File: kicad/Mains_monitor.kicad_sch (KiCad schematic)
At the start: 31 parts, among them J1 120VAC, J2 LOAD, K1 SANYOU_SRD_Form_C, Q1 NPN, Q2 BS170, T1 CST2010, U1 HLW8032

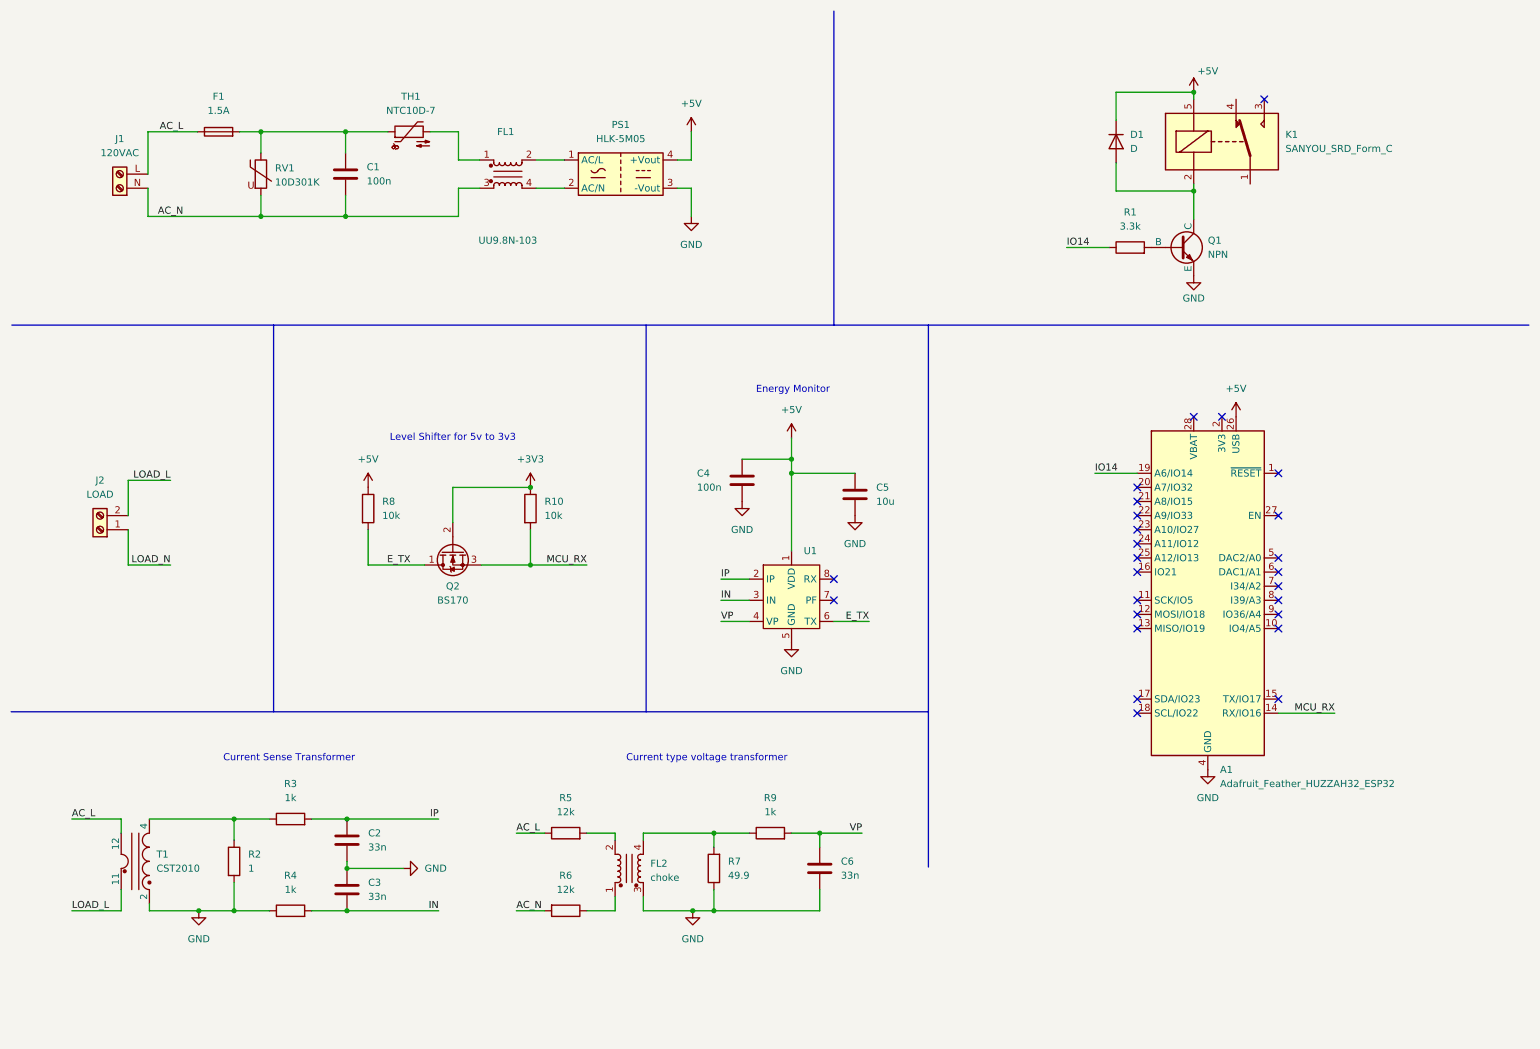
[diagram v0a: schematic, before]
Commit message: Improve sch clarity
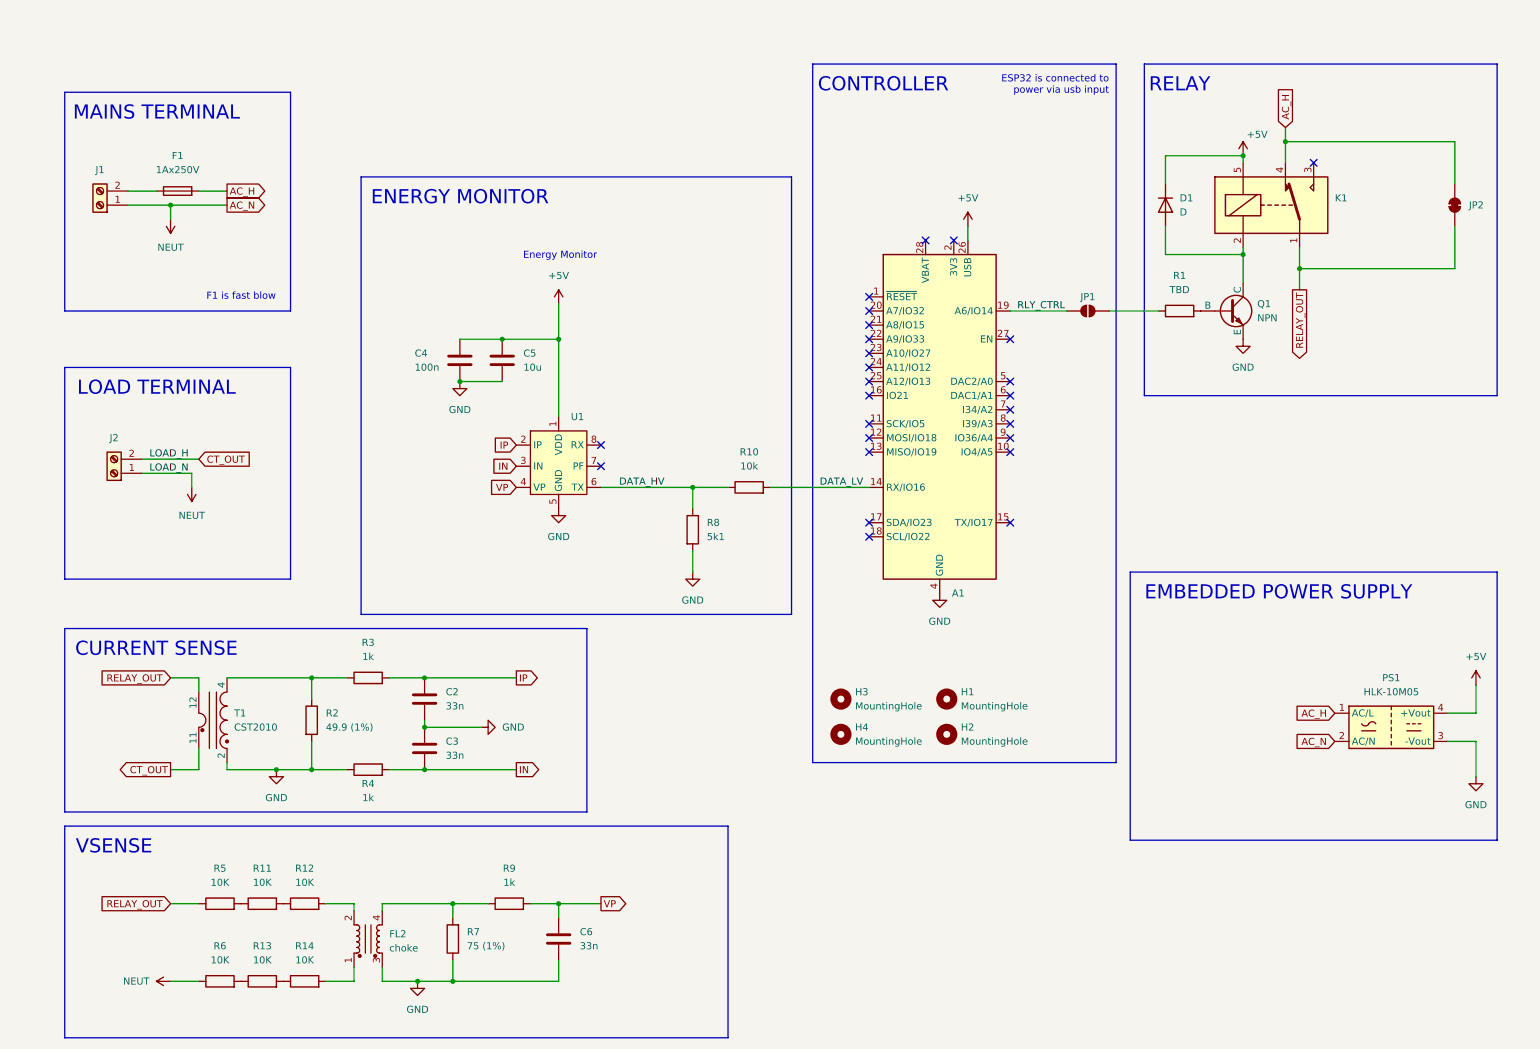
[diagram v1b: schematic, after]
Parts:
- removed C1: 100n, Capacitor_THT:C_Rect_L18.0mm_W5.0mm_P15.00mm_FKS3_FKP3, symbol Device:C
- removed FL1: UU9.8N-103, Inductor_THT:Choke_Schaffner_RN102-04-14.0x14.0mm, symbol Filter:Choke_Schaffner_RN102-0.3-02-12M
- removed PS1: HLK-5M05, Converter_ACDC:Converter_ACDC_Hi-Link_HLK-5Mxx, symbol Converter_ACDC:HLK-5M05
- removed Q2: BS170, Package_TO_SOT_THT:TO-92_Inline, symbol Transistor_FET:BS170
- removed RV1: 10D301K, symbol Device:Varistor
- removed TH1: NTC10D-7, symbol Device:Thermistor_NTC
- added H1, H2, H3, H4: MountingHole, symbol Mechanical:MountingHole
- added JP1: RELAY LOGIC BYPASS, symbol Jumper:SolderJumper_2_Open
- added JP2: SolderJumper_2_Bridged, symbol Jumper:SolderJumper_2_Bridged
- added PS1: HLK-10M05, Converter_ACDC:Converter_ACDC_Hi-Link_HLK-10Mxx, symbol Converter_ACDC:HLK-10M05
- added R11, R12, R13, R14: 10K, symbol Device:R
- F1: value 1.5A -> 1Ax250V
- J1: value 120VAC -> Screw_Terminal_01x02
- J2: value LOAD -> Screw_Terminal_01x02
- R1: value 3.3k -> TBD
- R2: value 1 -> 49.9 (1%)
- R5, R6: value 12k -> 10K
- R7: value 49.9 -> 75 (1%)
- R8: value 10k -> 5k1
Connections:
- net +5V: now also PS1.4 (+Vout); no longer R8.1
- net GND: now also R8.2, PS1.3 (-Vout)
- net AC_H: now reaches F1.2
- net AC_H: now also K1.4, JP2.2 (B), PS1.1 (AC/L)
- net at FL2.2: now also R12.2; no longer R5.2
- net at FL2.1: now also R14.2; no longer R6.1
- net RELAY_OUT: now reaches K1.1
- net RELAY_OUT: now also R5.1, T1.12, JP2.1 (A)
- net +3V3 renamed DATA_HV
- net DATA_HV: now also R8.1, U1.6 (TX)
- removed net AC_L: F1.1, J1.L (pin_2), R5.1, T1.12
- net AC_N: no longer names the net of R6.2
- net AC_N: now also R13.1; no longer J1.N (Pin_1)
- removed net E_TX: R8.2, U1.6 (TX)
- net IO14: no longer names the net of R1.1
- net IO14: now also JP1.2 (B); no longer A1.19 (A6/IO14)
- net LOAD_L renamed CT_OUT
- net LOAD_N renamed NEUT
- net NEUT: now also J1.1 (Pin_1), R6.1, PS1.2 (AC/N)
- net MCU_RX renamed DATA_LV
- new net: R11.2, R12.1
- new net: R11.1, R5.2
- new net: F1.1, J1.2 (Pin_2)
- new net: R13.2, R14.1
- new net RLY_CTRL: A1.19 (A6/IO14), JP1.1 (A)
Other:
- note added: "CONTROLLER"
- note added: "CURRENT SENSE"
- note added: "EMBEDDED POWER SUPPLY"
- note added: "ENERGY MONITOR"
- note added: "ESP32 is connected to power via usb input"
- note added: "F1 is fast blow"
- note added: "LOAD TERMINAL"
- note added: "MAINS TERMINAL"
- note added: "RELAY"
- note added: "VSENSE"
- note removed: "Current Sense Transformer"
- note removed: "Current type voltage transformer"
- note removed: "Level Shifter for 5v to 3v3"
- moved on the sheet: A1, C2, C3, C4, C5, C6, D1, FL2, K1, Q1, R1, R2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

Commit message: added footprints for all components, started PCB layout
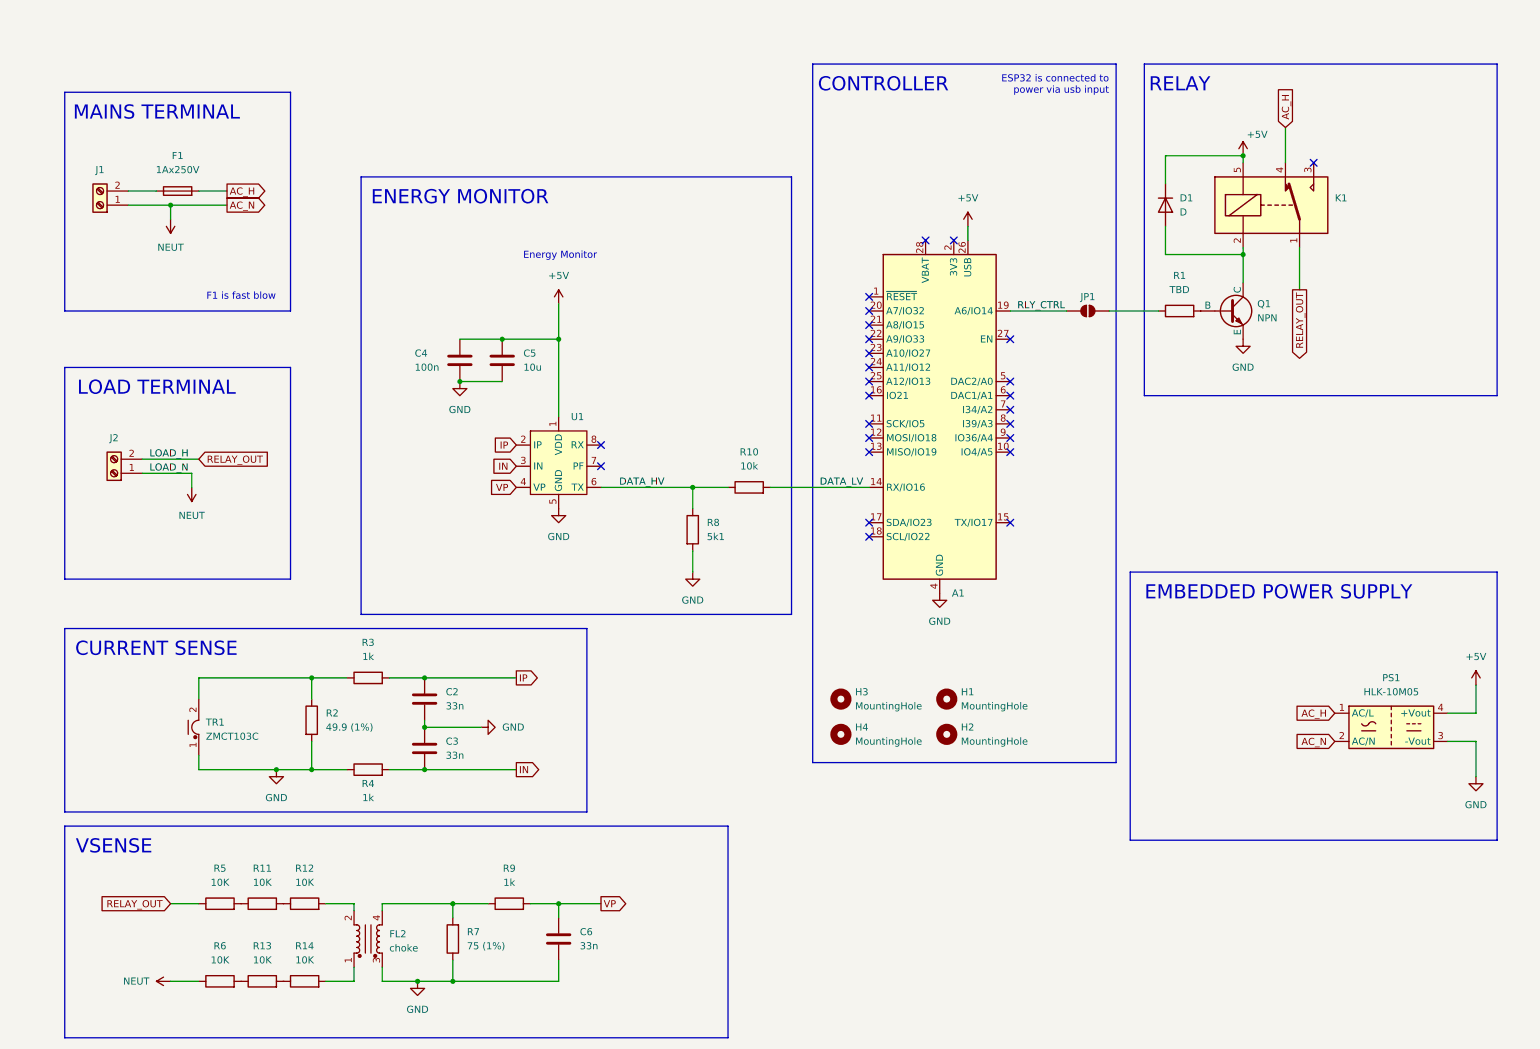
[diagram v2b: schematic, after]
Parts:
- removed JP2: SolderJumper_2_Bridged, symbol Jumper:SolderJumper_2_Bridged
- removed T1: CST2010, Transformer_SMD:Transformer_Coilcraft_CST2010, symbol Transformer:CST2010
- added TR1: ZMCT103C, Transformer_THT:Transformer_Zeming_ZMCT103C, symbol Transformer:ZMCT103C
- C2, C3, C4, C5, C6: footprint Capacitor_SMD:C_0805_2012Metric_Pad1.18x1.45mm_HandSolder -> Capacitor_THT:C_Radial_D5.0mm_H7.0mm_P2.00mm
- D1: footprint (none) -> Diode_THT:D_A-405_P7.62mm_Horizontal
- F1: footprint (none) -> Fuse:Fuseholder_Clip-5x20mm_Bel_FC-203-22_Lateral_P17.80x5.00mm_D1.17mm_Horizontal
- J1, J2: footprint (none) -> Connector_Screw_Terminal:CONN2_020000_WED
- JP1: footprint (none) -> Jumper:SolderJumper-2_P1.3mm_Open_RoundedPad1.0x1.5mm
- Q1: footprint (none) -> Package_TO_SOT_THT:TO-92_Inline
- R1, R10, R11, R12, R13, R14, R2, R3, R4, R5, R6, R7, R8, R9: footprint (none) -> Resistor_THT:R_Axial_DIN0207_L6.3mm_D2.5mm_P10.16mm_Horizontal
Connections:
- net CT_OUT is gone; now on net RELAY_OUT: J2.2 (Pin_2)
- net GND: now also TR1.1
- net at R2.1, R3.1: now also TR1.2

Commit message: added mounting holes and ground layers
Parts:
- H1, H2, H3, H4: footprint (none) -> MountingHole:MountingHole_5.3mm_M5
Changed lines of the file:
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@@
 			)
 		)
-		(property "Footprint" ""
+		(property "Footprint" "MountingHole:MountingHole_5.3mm_M5"
 			(at 180.34 135.89 0)
 			(effects
@@
 			)
 		)
-		(property "Footprint" ""
+		(property "Footprint" "MountingHole:MountingHole_5.3mm_M5"
 			(at 161.29 135.89 0)
 			(effects
@@
 			)
 		)
-		(property "Footprint" ""
+		(property "Footprint" "MountingHole:MountingHole_5.3mm_M5"
 			(at 180.34 142.24 0)
 			(effects
@@
 			)
 		)
-		(property "Footprint" ""
+		(property "Footprint" "MountingHole:MountingHole_5.3mm_M5"
 			(at 161.29 142.24 0)
 			(effects

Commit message: added net class for 120V and mounting holes
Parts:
- H1, H2, H3, H4: footprint MountingHole:MountingHole_5.3mm_M5 -> MountingHole:MountingHole_3.5mm
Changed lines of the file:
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@@
 		)
 	)
+	(netclass_flag ""
+		(length 2.54)
+		(shape round)
+		(at 48.26 44.45 0)
+		(fields_autoplaced yes)
+		(effects
+			(font
+				(size 1.27 1.27)
+			)
+			(justify left bottom)
+		)
+		(property "Netclass" "120V"
+			(at 48.9585 41.91 0)
+			(effects
+				(font
+					(size 1.27 1.27)
+					(italic yes)
+				)
+				(justify left)
+			)
+		)
+	)
+	(netclass_flag ""
+		(length 2.54)
+		(shape round)
+		(at 34.29 44.45 0)
+		(fields_autoplaced yes)
+		(effects
+			(font
+				(size 1.27 1.27)
+			)
+			(justify left bottom)
+		)
+		(property "Netclass" "120V"
+			(at 34.9885 41.91 0)
+			(effects
+				(font
+					(size 1.27 1.27)
+					(italic yes)
+				)
+				(justify left)
+			)
+		)
+	)
+	(netclass_flag ""
+		(length 2.54)
+		(shape round)
+		(at 45.72 46.99 180)
+		(fields_autoplaced yes)
+		(effects
+			(font
+				(size 1.27 1.27)
+			)
+			(justify right bottom)
+		)
+		(property "Netclass" "120V"
+			(at 46.4185 49.53 0)
+			(effects
+				(font
+					(size 1.27 1.27)
+					(italic yes)
+				)
+				(justify left)
+			)
+		)
+	)
+	(netclass_flag ""
+		(length 2.54)
+		(shape round)
+		(at 44.45 92.71 0)
+		(fields_autoplaced yes)
+		(effects
+			(font
+				(size 1.27 1.27)
+			)
+			(justify left bottom)
+		)
+		(property "Netclass" "120V"
+			(at 45.1485 90.17 0)
+			(effects
+				(font
+					(size 1.27 1.27)
+					(italic yes)
+				)
+				(justify left)
+			)
+		)
+	)
 	(symbol
 		(lib_id "Device:C")
@@
 			)
 		)
-		(property "Footprint" "MountingHole:MountingHole_5.3mm_M5"
+		(property "Footprint" "MountingHole:MountingHole_3.5mm"
 			(at 180.34 135.89 0)
 			(effects
@@
 			)
 		)
-		(property "Footprint" "MountingHole:MountingHole_5.3mm_M5"
+		(property "Footprint" "MountingHole:MountingHole_3.5mm"
 			(at 161.29 135.89 0)
 			(effects
@@
 			)
 		)
-		(property "Footprint" "MountingHole:MountingHole_5.3mm_M5"
+		(property "Footprint" "MountingHole:MountingHole_3.5mm"
 			(at 180.34 142.24 0)
 			(effects
@@
 			)
 		)
-		(property "Footprint" "MountingHole:MountingHole_5.3mm_M5"
+		(property "Footprint" "MountingHole:MountingHole_3.5mm"
 			(at 161.29 142.24 0)
 			(effects
